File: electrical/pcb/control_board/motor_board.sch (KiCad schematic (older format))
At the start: 92 parts

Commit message: add inter board connector
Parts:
- added J26: PEC10DAAN, symbol JPL_Robotics_Lib:PEC10DAAN
- gave numbers to parts that had none: 92
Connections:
- wire segments 377 -> 383
- no-connect marks 93 -> 106
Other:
- note added: "Inter-Board Connection"
- moved on the sheet: C1, C13, C14, C2, C3, C4, D1, F1, J1, J10, J2, J3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

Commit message: moving mounting holes, unnumbering inter board connectors, and adding to kicad readme
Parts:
- added M?: Mounting_Holes, JPL Robotics:Raspberry pi footprint, symbol JPL_Robotics_Lib:Mounting_Holes
- added MH? (x4): #6THRU-HOLE, JPL Robotics:#6THRU-HOLE, symbol JPL_Robotics_Lib:#6THRU-HOLE
- added y?: rover_silkscreen, JPL Robotics:rover_image, symbol JPL_Robotics_Lib:rover_silkscreen
- renumbered J26 to J?
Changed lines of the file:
@@
 	15550 5400 15550 9300
 $Comp
-L JPL_Robotics_Lib:PEC10DAAN J26
+L JPL_Robotics_Lib:PEC10DAAN J?
 U 1 1 6099FCA6
 P 14300 6850
-F 0 "J26" H 14300 6925 50  0000 C CNN
+F 0 "J?" H 14300 6925 50  0000 C CNN
 F 1 "PEC10DAAN" H 14300 6834 50  0000 C CNN
 F 2 "" H 14500 6850 50  0001 C CNN
@@
 NoConn ~ 14050 7900
 NoConn ~ 14550 7300
+$Comp
+L JPL_Robotics_Lib:Mounting_Holes M?
+U 1 1 609530FB
+P 1100 9900
+F 0 "M?" V 1530 10079 30  0000 L CNN
+F 1 "Mounting_Holes" V 1590 10079 30  0000 L CNN
+F 2 "JPL Robotics:Raspberry pi footprint" H 1280 10080 30  0001 C CNN
+F 3 "" H 1280 10080 30  0001 C CNN
+	1    1100 9900
+	0    1    1    0
+$EndComp
+$Comp
+L JPL_Robotics_Lib:#6THRU-HOLE MH?
+U 1 1 60953101
+P 1950 9950
+F 0 "MH?" H 2081 9950 30  0000 L CNN
+F 1 "#6THRU-HOLE" H 1950 10090 30  0001 C CNN
+F 2 "JPL Robotics:#6THRU-HOLE" H 1950 10040 30  0001 C CNN
+F 3 "" H 1950 10040 30  0001 C CNN
+	1    1950 9950
+	1    0    0    -1
+$EndComp
+$Comp
+L JPL_Robotics_Lib:#6THRU-HOLE MH?
+U 1 1 60953107
+P 1950 10100
+F 0 "MH?" H 2081 10100 30  0000 L CNN
+F 1 "#6THRU-HOLE" H 1950 10240 30  0001 C CNN
+F 2 "JPL Robotics:#6THRU-HOLE" H 1950 10190 30  0001 C CNN
+F 3 "" H 1950 10190 30  0001 C CNN
+	1    1950 10100
+	1    0    0    -1
+$EndComp
+$Comp
+L JPL_Robotics_Lib:#6THRU-HOLE MH?
+U 1 1 6095310D
+P 1950 10250
+F 0 "MH?" H 2081 10250 30  0000 L CNN
+F 1 "#6THRU-HOLE" H 1950 10390 30  0001 C CNN
+F 2 "JPL Robotics:#6THRU-HOLE" H 1950 10340 30  0001 C CNN
+F 3 "" H 1950 10340 30  0001 C CNN
+	1    1950 10250
+	1    0    0    -1
+$EndComp
+$Comp
+L JPL_Robotics_Lib:#6THRU-HOLE MH?
+U 1 1 60953113
+P 1950 10400
+F 0 "MH?" H 2081 10400 30  0000 L CNN
+F 1 "#6THRU-HOLE" H 1950 10540 30  0001 C CNN
+F 2 "JPL Robotics:#6THRU-HOLE" H 1950 10490 30  0001 C CNN
+F 3 "" H 1950 10490 30  0001 C CNN
+	1    1950 10400
+	1    0    0    -1
+$EndComp
+$Comp
+L JPL_Robotics_Lib:rover_silkscreen y?
+U 1 1 60953119
+P 1100 10750
+F 0 "y?" H 1278 10825 50  0000 L CNN
+F 1 "rover_silkscreen" H 1278 10780 50  0000 L CNN
+F 2 "JPL Robotics:rover_image" H 950 10850 50  0001 C CNN
+F 3 "" H 950 10850 50  0001 C CNN
+	1    1100 10750
+	1    0    0    -1
+$EndComp
 $EndSCHEMATC

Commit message: Fix numbering to align with component ref designators before splitting into multiple sheets, add numbering for new inter-board connectors
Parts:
- gave numbers to parts that had none: 7
- renumbered C21 to C10, C22 to C11, C3 to C12, C4 to C13, C13 to C14, C14 to C15, C1 to C16, C2 to C17, C23 to C19, C7 to C2, C26 to C20, C24 to C21, C27 to C22, C5 to C23, C6 to C24, C11 to C25, C12 to C26, C19 to C27, C20 to C28, C25 to C29, C8 to C3, C28 to C30, C9 to C4, C10 to C5, C15 to C6, C16 to C7, C17 to C8, C18 to C9, J11 to J1, J10 to J11, J5 to J13, J1 to J14, J2 to J15, J6 to J16, J16 to J17, J17 to J18, J18 to J19, J12 to J2, J19 to J20, J20 to J21, J21 to J22, J22 to J23, J23 to J24, J24 to J25, J25 to J26, J8 to J28, J4 to J29, J13 to J3, J7 to J30, J3 to J31, J14 to J4, J15 to J5, R9 to R10, R1 to R2, R2 to R3, R3 to R4, R4 to R5, R5 to R6, R6 to R7, R7 to R8, R8 to R9, T3 to T2, T2 to T3

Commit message: updating motor and brain boards with board-specific power nets
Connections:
- net labels added: +12V_motor, +5V_motor, GND_motor
- net labels removed: +12V, +5V, GND
- wire segments 383 -> 382
- no-connect marks 106 -> 107
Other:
- moved on the sheet: C10, C11, C13, C15, C19, C2, C20, C21, C22, C23, C24, C25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

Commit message: Adding footprints for male and female inter-board connectors
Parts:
- J12: footprint (none) -> JPL Robotics:PEC10DAAN
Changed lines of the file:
@@
 F 0 "J12" H 14300 6925 50  0000 C CNN
 F 1 "PEC10DAAN" H 14300 6834 50  0000 C CNN
-F 2 "" H 14500 6850 50  0001 C CNN
+F 2 "JPL Robotics:PEC10DAAN" H 14500 6850 50  0001 C CNN
 F 3 "" H 14500 6850 50  0001 C CNN
 	1    14300 6850

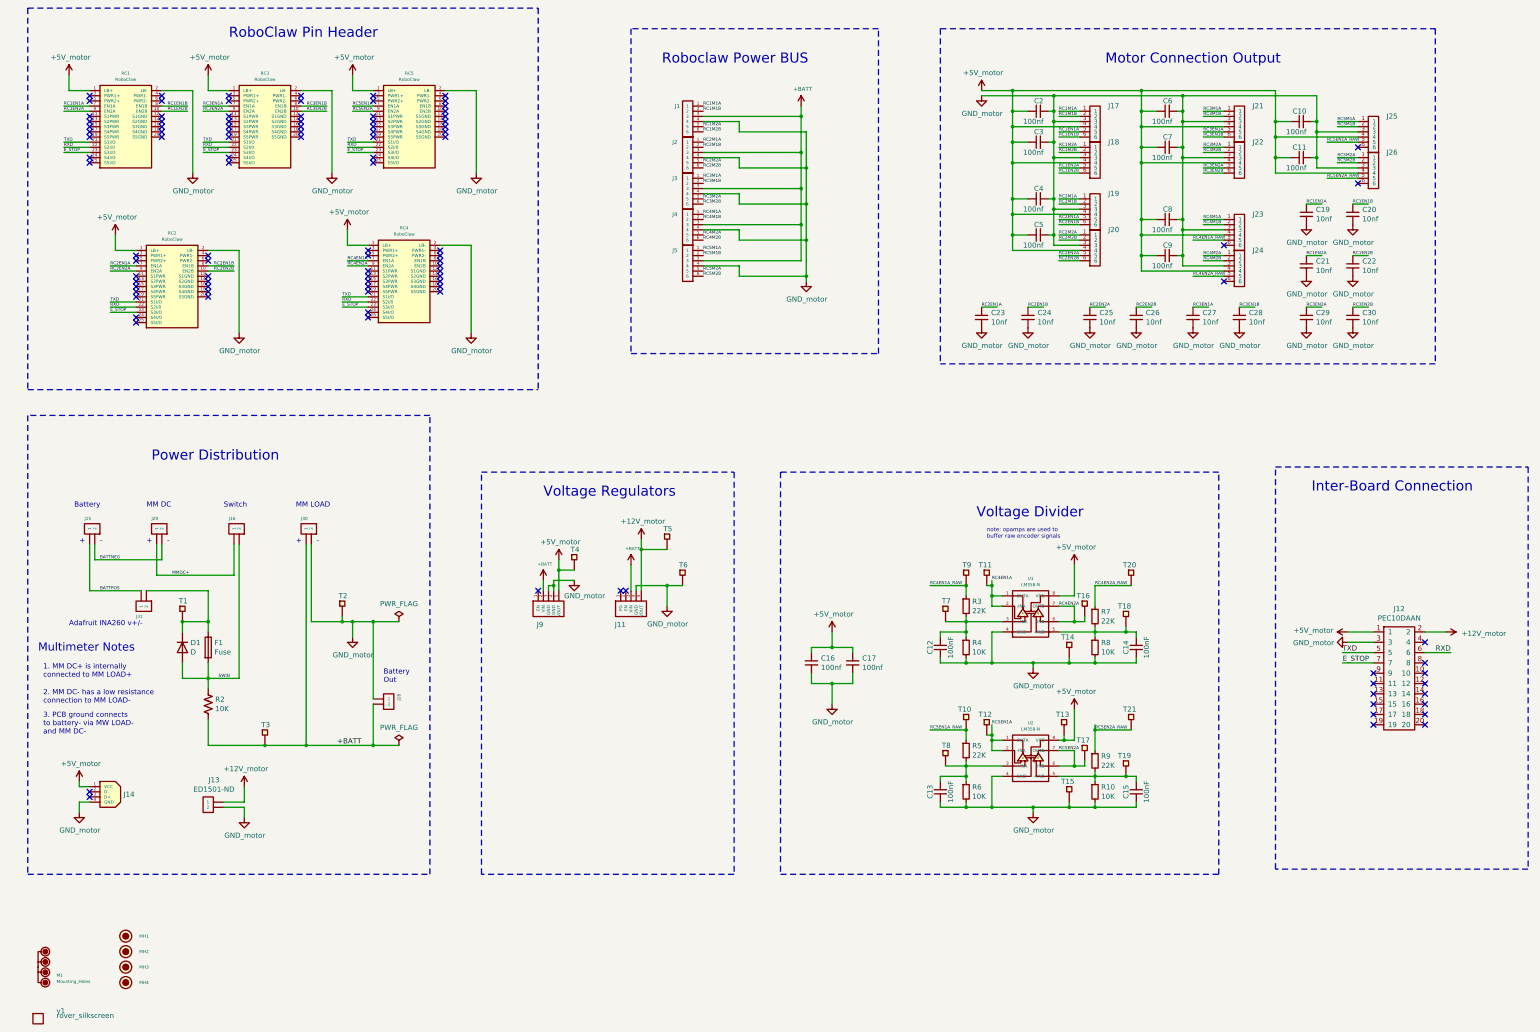
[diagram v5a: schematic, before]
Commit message: Adding secondary e-stop line connected to s4 on roboclaw, along with a 2 pin header for it on the brain board
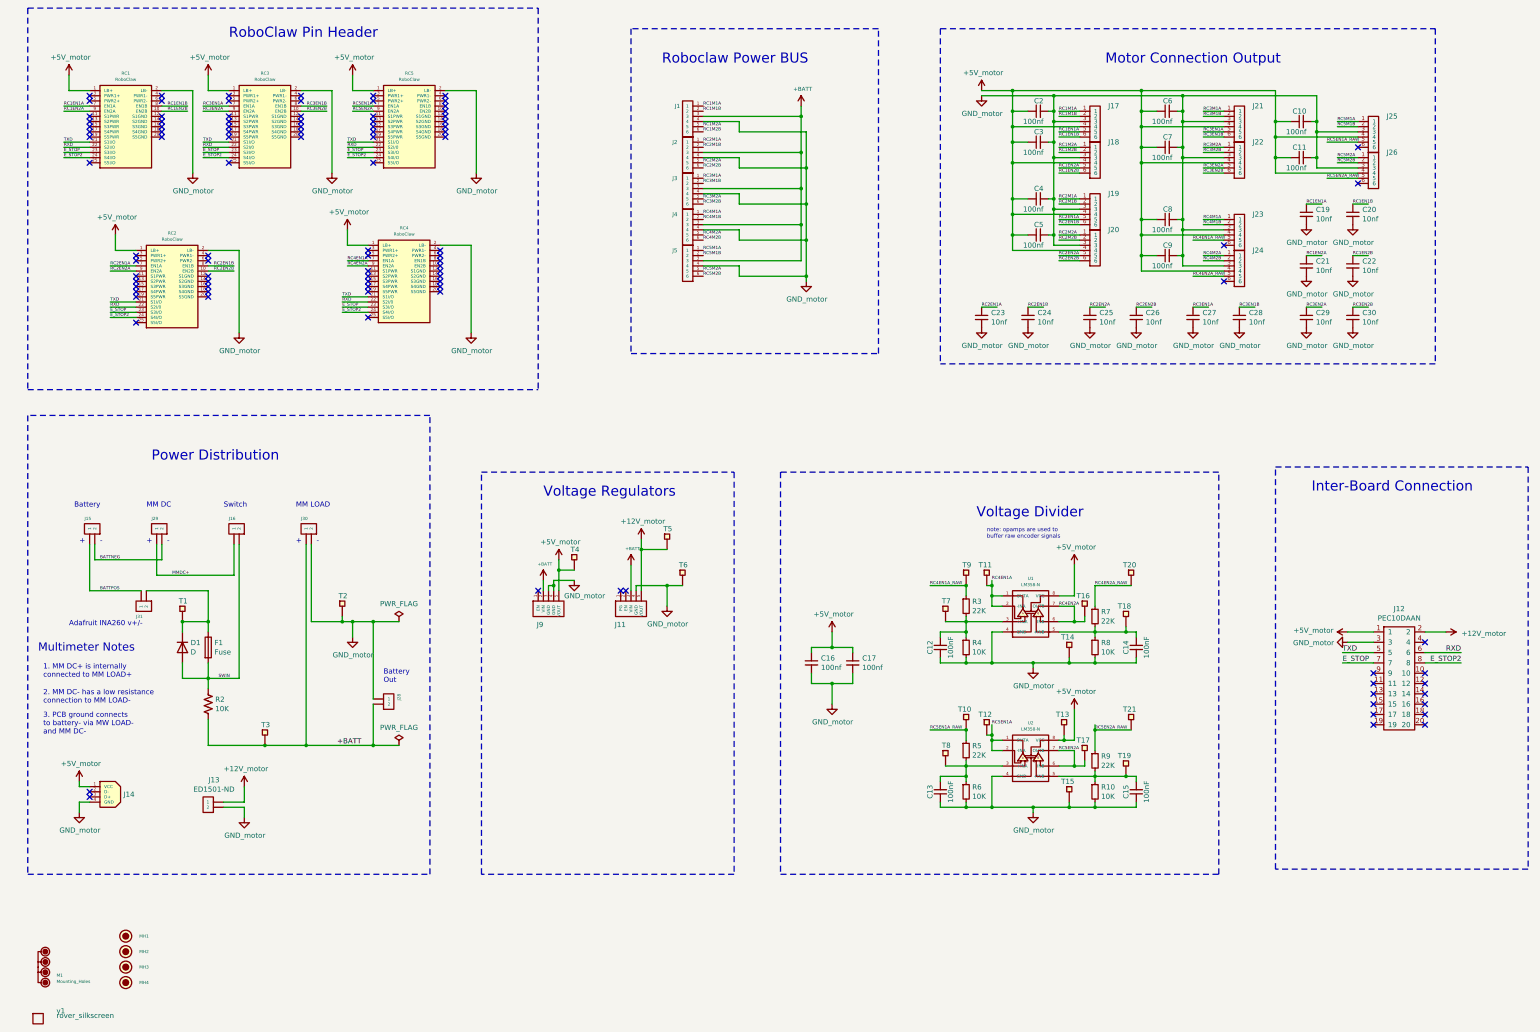
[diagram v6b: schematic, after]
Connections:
- net labels added: E_STOP2
- wire segments 382 -> 388
- no-connect marks 107 -> 101
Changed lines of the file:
@@
 Text Label 4100 2300 0    30   ~ 0
 RXD
-$Comp
-L JPL_Robotics_Lib:RoboClaw RC?
-U 1 1 60AB7B1E
-P 2150 4050
-AR Path="/60AB7B1E" Ref="RC?"  Part="1"
-AR Path="/60A51BAC/60AB7B1E" Ref="RC2"  Part="1"
-F 0 "RC2" H 2400 4968 30  0000 C CNN
-F 1 "RoboClaw" H 2400 4908 30  0000 C CNN
-F 2 "JPL Robotics:Roboclaw Mount" H 2400 4950 30  0001 C CNN
-F 3 "" H 2400 4950 30  0001 C CNN
-	1    2150 4050
-	1    0    0    -1
-$EndComp
 Wire Wire Line
 	1850 3150 1850 3300
@@
 NoConn ~ 1600 2150
 NoConn ~ 1600 2200
-NoConn ~ 1600 2400
 NoConn ~ 1600 2450
 NoConn ~ 2950 1800
@@
 NoConn ~ 2950 2150
 NoConn ~ 2950 2200
-NoConn ~ 2950 2400
 NoConn ~ 2950 2450
 NoConn ~ 3650 1800
@@
 NoConn ~ 4350 2150
 NoConn ~ 4350 2200
-NoConn ~ 4350 2400
 NoConn ~ 4350 2450
 NoConn ~ 5050 1800
@@
 NoConn ~ 2050 3700
 NoConn ~ 2050 3750
-NoConn ~ 2050 3950
 NoConn ~ 2050 4000
 NoConn ~ 2750 3350
@@
 NoConn ~ 4300 3650
 NoConn ~ 4300 3700
-NoConn ~ 4300 3900
 NoConn ~ 4300 3950
 NoConn ~ 5000 3300
@@
 	14550 7000 14750 7000
 Wire Wire Line
-	14550 7200 14800 7200
-Wire Wire Line
 	13750 7300 14050 7300
 Wire Wire Line
@@
 Text Label 13750 7300 0    50   ~ 0
 E_STOP
-Text Label 14800 7200 2    50   ~ 0
+Text Label 14900 7200 2    50   ~ 0
 RXD
 Text Label 13750 7200 0    50   ~ 0
@@
 NoConn ~ 14050 7800
 NoConn ~ 14050 7900
-NoConn ~ 14550 7300
 $Comp
 L JPL_Robotics_Lib:Mounting_Holes M1
@@
 Wire Notes Line style solid rgb(0, 0, 0)
 	9850 1150 9850 4400
+Wire Wire Line
+	14550 7300 14900 7300
+Text Label 14600 7300 0    50   ~ 0
+E_STOP2
+Wire Wire Line
+	14550 7200 14900 7200
+Wire Wire Line
+	1600 2400 1350 2400
+Text Label 1350 2400 0    30   ~ 0
+E_STOP2
+$Comp
+L JPL_Robotics_Lib:RoboClaw RC?
+U 1 1 60AB7B1E
+P 2150 4050
+AR Path="/60AB7B1E" Ref="RC?"  Part="1"
+AR Path="/60A51BAC/60AB7B1E" Ref="RC2"  Part="1"
+F 0 "RC2" H 2400 4968 30  0000 C CNN
+F 1 "RoboClaw" H 2400 4908 30  0000 C CNN
+F 2 "JPL Robotics:Roboclaw Mount" H 2400 4950 30  0001 C CNN
+F 3 "" H 2400 4950 30  0001 C CNN
+	1    2150 4050
+	1    0    0    -1
+$EndComp
+Wire Wire Line
+	2050 3950 1800 3950
+Text Label 1800 3950 0    30   ~ 0
+E_STOP2
+Wire Wire Line
+	2950 2400 2700 2400
+Text Label 2700 2400 0    30   ~ 0
+E_STOP2
+Wire Wire Line
+	4350 2400 4100 2400
+Text Label 4100 2400 0    30   ~ 0
+E_STOP2
+Wire Wire Line
+	4300 3900 4050 3900
+Text Label 4050 3900 0    30   ~ 0
+E_STOP2
 $EndSCHEMATC

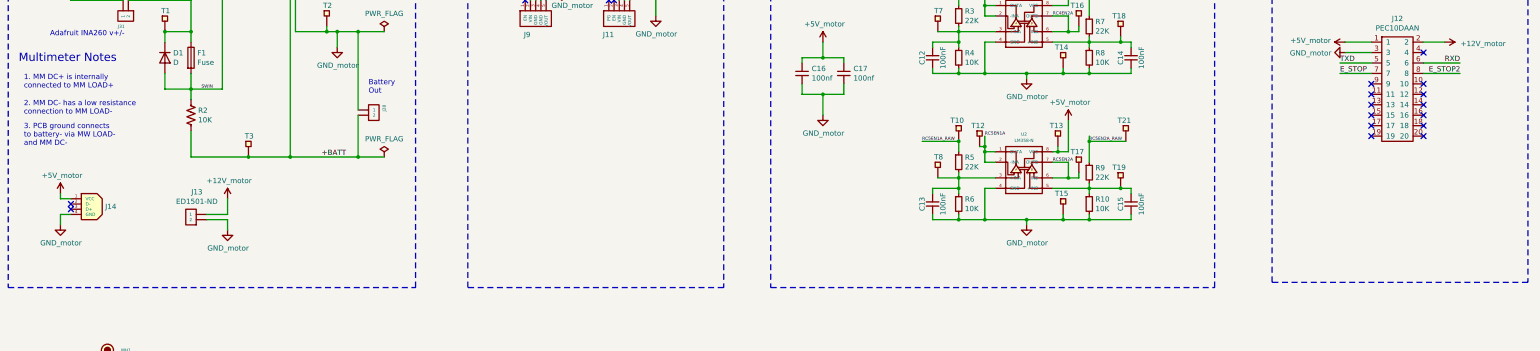
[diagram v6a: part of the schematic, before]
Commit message: Adding headers and rpi connections for gst
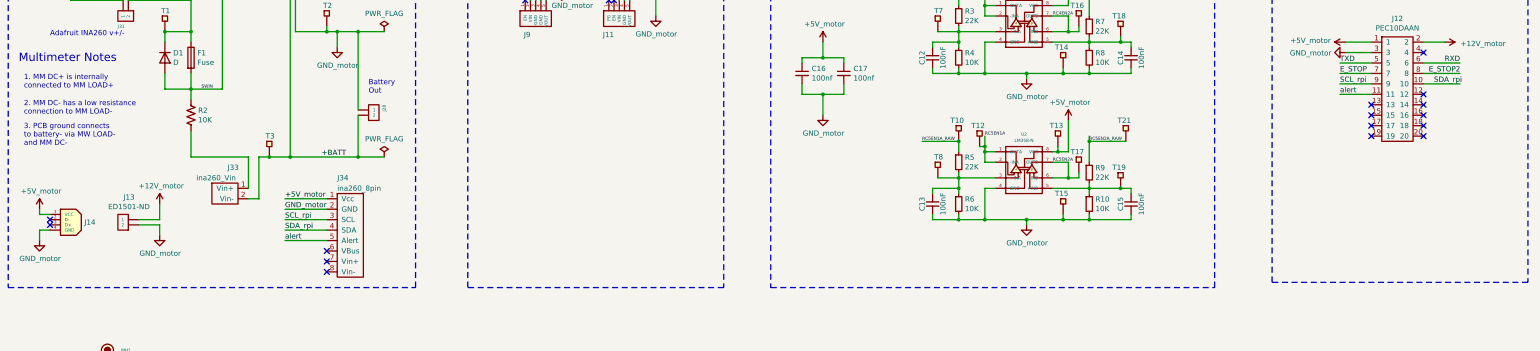
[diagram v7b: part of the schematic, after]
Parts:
- added J33: ina260_Vin, symbol JPL_Robotics_Lib:TSW-202-07-T-S_ina260
- added J34: ina260_8pin, symbol JPL_Robotics_Lib:PEC08SAAN_ina260
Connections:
- net labels added: SCL_rpi, SDA_rpi, alert
- wire segments 388 -> 400
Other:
- moved on the sheet: J13, J14, T3
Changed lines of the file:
@@
 L JPL_Robotics_Lib:test_point T?
 U 1 1 60B753AF
-P 3300 7950
+P 3500 7950
 AR Path="/60B753AF" Ref="T?"  Part="1"
 AR Path="/60A51BAC/60B753AF" Ref="T3"  Part="1"
-F 0 "T3" V 3350 7900 50  0000 L CNN
-F 1 "test_point" H 3450 8200 50  0001 C CNN
-F 2 "TestPoint:TestPoint_Pad_1.0x1.0mm" H 3250 7900 50  0001 C CNN
-F 3 "" H 3250 7900 50  0001 C CNN
-	1    3300 7950
+F 0 "T3" V 3550 7900 50  0000 L CNN
+F 1 "test_point" H 3650 8200 50  0001 C CNN
+F 2 "TestPoint:TestPoint_Pad_1.0x1.0mm" H 3450 7900 50  0001 C CNN
+F 3 "" H 3450 7900 50  0001 C CNN
+	1    3500 7950
 	0    -1   -1   0
 $EndComp
@@
 	4150 7050 4150 6900
 Wire Wire Line
-	1500 8650 1500 8750
+	1300 8800 1300 8900
 $Comp
 L Device:R_US R?
@@
 	6850 6350 6850 6600
 Wire Wire Line
-	2900 8650 3100 8650
-Wire Wire Line
-	2900 8700 3100 8700
-Wire Wire Line
-	3100 8700 3100 8800
-Wire Wire Line
-	3100 8500 3100 8650
+	2250 8700 2450 8700
+Wire Wire Line
+	2250 8750 2450 8750
+Wire Wire Line
+	2450 8750 2450 8850
+Wire Wire Line
+	2450 8550 2450 8700
 $Comp
 L JPL_Robotics_Lib:test_point T?
@@
 L JPL_Robotics_Lib:ED2989-ND-USB J?
 U 1 1 60B754FB
-P 1450 8650
+P 1250 8800
 AR Path="/60B754FB" Ref="J?"  Part="1"
 AR Path="/60A51BAC/60B754FB" Ref="J14"  Part="1"
-F 0 "J14" H 1928 8725 50  0000 L CNN
-F 1 "ED2989-ND-USB" H 1927 8680 50  0001 L CNN
-F 2 "JPL Robotics:ED2989-ND USB Conn" H 1450 8650 50  0001 C CNN
-F 3 "" H 1450 8650 50  0001 C CNN
-	1    1450 8650
-	1    0    0    -1
-$EndComp
-Wire Wire Line
-	1600 8500 1500 8500
-Wire Wire Line
-	1500 8500 1500 8450
-Wire Wire Line
-	1600 8650 1500 8650
+F 0 "J14" H 1728 8875 50  0000 L CNN
+F 1 "ED2989-ND-USB" H 1727 8830 50  0001 L CNN
+F 2 "JPL Robotics:ED2989-ND USB Conn" H 1250 8800 50  0001 C CNN
+F 3 "" H 1250 8800 50  0001 C CNN
+	1    1250 8800
+	1    0    0    -1
+$EndComp
+Wire Wire Line
+	1400 8650 1300 8650
+Wire Wire Line
+	1300 8650 1300 8600
+Wire Wire Line
+	1400 8800 1300 8800
 $Comp
 L JPL_Robotics_Lib:ED1501-ND J?
 U 1 1 60B75504
-P 2700 8750
+P 2050 8800
 AR Path="/60B75504" Ref="J?"  Part="1"
 AR Path="/60A51BAC/60B75504" Ref="J13"  Part="1"
-F 0 "J13" H 2806 9065 50  0000 C CNN
-F 1 "ED1501-ND" H 2806 8974 50  0000 C CNN
-F 2 "JPL Robotics:ED1501-ND" H 2700 8750 50  0001 C CNN
-F 3 "" H 2700 8750 50  0001 C CNN
-	1    2700 8750
+F 0 "J13" H 2156 9115 50  0000 C CNN
+F 1 "ED1501-ND" H 2156 9024 50  0000 C CNN
+F 2 "JPL Robotics:ED1501-ND" H 2050 8800 50  0001 C CNN
+F 3 "" H 2050 8800 50  0001 C CNN
+	1    2050 8800
 	1    0    0    -1
 $EndComp
@@
 	3750 6150 3750 6900
 Wire Wire Line
-	2750 8100 3300 8100
-Wire Wire Line
 	3050 7450 2750 7450
 Wire Wire Line
@@
 Text Notes 1150 7700 0    50   ~ 0
 2. MM DC- has a low resistance \nconnection to MM LOAD-
-Connection ~ 3300 8100
-Wire Wire Line
-	3300 8100 3700 8100
 Wire Wire Line
 	3700 6150 3700 8100
@@
 Text Notes 10300 6100 0    39   ~ 0
 note: opamps are used to \nbuffer raw encoder signals
-NoConn ~ 1600 8550
-NoConn ~ 1600 8600
+NoConn ~ 1400 8700
+NoConn ~ 1400 8750
 $Comp
 L JPL_Robotics_Lib:S7038-ND_regulator_D24V50F5 J?
@@
 	1    0    0    -1
 $EndComp
-NoConn ~ 14550 7400
 NoConn ~ 14550 7500
 NoConn ~ 14550 7600
@@
 NoConn ~ 14550 7800
 NoConn ~ 14550 7900
-NoConn ~ 14050 7400
-NoConn ~ 14050 7500
 NoConn ~ 14050 7600
 NoConn ~ 14050 7700
@@
 L JPL_Robotics_Lib:GND_motor #PWR0127
 U 1 1 6131E13D
-P 1500 8750
-F 0 "#PWR0127" H 1500 8500 50  0001 C CNN
-F 1 "GND_motor" H 1505 8577 50  0000 C CNN
-F 2 "" H 1500 8750 50  0001 C CNN
-F 3 "" H 1500 8750 50  0001 C CNN
-	1    1500 8750
+P 1300 8900
+F 0 "#PWR0127" H 1300 8650 50  0001 C CNN
+F 1 "GND_motor" H 1305 8727 50  0000 C CNN
+F 2 "" H 1300 8900 50  0001 C CNN
+F 3 "" H 1300 8900 50  0001 C CNN
+	1    1300 8900
 	1    0    0    -1
 $EndComp
@@
 L JPL_Robotics_Lib:GND_motor #PWR0128
 U 1 1 61347F19
-P 3100 8800
-F 0 "#PWR0128" H 3100 8550 50  0001 C CNN
-F 1 "GND_motor" H 3105 8627 50  0000 C CNN
-F 2 "" H 3100 8800 50  0001 C CNN
-F 3 "" H 3100 8800 50  0001 C CNN
-	1    3100 8800
+P 2450 8850
+F 0 "#PWR0128" H 2450 8600 50  0001 C CNN
+F 1 "GND_motor" H 2455 8677 50  0000 C CNN
+F 2 "" H 2450 8850 50  0001 C CNN
+F 3 "" H 2450 8850 50  0001 C CNN
+	1    2450 8850
 	1    0    0    -1
 $EndComp
@@
 L JPL_Robotics_Lib:+5V_motor #PWR0129
 U 1 1 6139B9A5
-P 1500 8450
-F 0 "#PWR0129" H 1500 8300 50  0001 C CNN
-F 1 "+5V_motor" H 1515 8623 50  0000 C CNN
-F 2 "" H 1500 8450 50  0001 C CNN
-F 3 "" H 1500 8450 50  0001 C CNN
-	1    1500 8450
+P 1300 8600
+F 0 "#PWR0129" H 1300 8450 50  0001 C CNN
+F 1 "+5V_motor" H 1315 8773 50  0000 C CNN
+F 2 "" H 1300 8600 50  0001 C CNN
+F 3 "" H 1300 8600 50  0001 C CNN
+	1    1300 8600
 	1    0    0    -1
 $EndComp
@@
 L JPL_Robotics_Lib:+12V_motor #PWR0130
 U 1 1 613EFE54
-P 3100 8500
-F 0 "#PWR0130" H 3100 8350 50  0001 C CNN
-F 1 "+12V_motor" H 3115 8673 50  0000 C CNN
-F 2 "" H 3100 8500 50  0001 C CNN
-F 3 "" H 3100 8500 50  0001 C CNN
-	1    3100 8500
+P 2450 8550
+F 0 "#PWR0130" H 2450 8400 50  0001 C CNN
+F 1 "+12V_motor" H 2465 8723 50  0000 C CNN
+F 2 "" H 2450 8550 50  0001 C CNN
+F 3 "" H 2450 8550 50  0001 C CNN
+	1    2450 8550
 	1    0    0    -1
 $EndComp
@@
 Text Label 4050 3900 0    30   ~ 0
 E_STOP2
+$Comp
+L JPL_Robotics_Lib:PEC08SAAN_ina260 J34
+U 1 1 609FD195
+P 4400 8350
+F 0 "J34" H 4150 8400 50  0000 L CNN
+F 1 "ina260_8pin" H 4150 8300 50  0000 L CNN
+F 2 "" H 4450 8350 50  0001 C CNN
+F 3 "" H 4450 8350 50  0001 C CNN
+	1    4400 8350
+	1    0    0    -1
+$EndComp
+$Comp
+L JPL_Robotics_Lib:TSW-202-07-T-S_ina260 J33
+U 1 1 609F9A06
+P 3100 8250
+F 0 "J33" H 3100 8300 50  0000 L CNN
+F 1 "ina260_Vin" H 2800 8200 50  0000 L CNN
+F 2 "" H 3150 8250 50  0001 C CNN
+F 3 "" H 3150 8250 50  0001 C CNN
+	1    3100 8250
+	1    0    0    -1
+$EndComp
+Connection ~ 3500 8100
+Wire Wire Line
+	3500 8100 3700 8100
+Wire Wire Line
+	3300 8100 3300 8400
+Wire Wire Line
+	3400 8500 3400 8100
+Wire Wire Line
+	3400 8100 3500 8100
+Wire Wire Line
+	2750 8100 3300 8100
+Wire Wire Line
+	3300 8500 3400 8500
+Text Label 3650 8500 0    50   ~ 0
++5V_motor
+Wire Wire Line
+	3650 8500 4050 8500
+Text Label 3650 8600 0    50   ~ 0
+GND_motor
+Wire Wire Line
+	3650 8600 4050 8600
+Wire Wire Line
+	14050 7400 13750 7400
+Text Label 13750 7400 0    50   ~ 0
+SCL_rpi
+Wire Wire Line
+	14550 7400 14900 7400
+Text Label 14650 7400 0    50   ~ 0
+SDA_rpi
+Wire Wire Line
+	4050 8700 3650 8700
+Text Label 3650 8700 0    50   ~ 0
+SCL_rpi
+Wire Wire Line
+	4050 8800 3650 8800
+Text Label 3650 8800 0    50   ~ 0
+SDA_rpi
+NoConn ~ 4050 9000
+NoConn ~ 4050 9100
+NoConn ~ 4050 9200
+Wire Wire Line
+	14050 7500 13750 7500
+Text Label 13750 7500 0    50   ~ 0
+alert
+Wire Wire Line
+	4050 8900 3650 8900
+Text Label 3650 8900 0    50   ~ 0
+alert
 $EndSCHEMATC
